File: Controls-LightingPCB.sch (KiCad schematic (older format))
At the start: 14 parts, among them J1 MinionConn, U1 LTC6820, U2 HX1188FNL

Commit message: Fixing merge issues
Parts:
- LOGO1, LOGO2: symbol utsvt-misc:Logo_Placeholder -> Controls-LightingPCB-rescue:Logo_Placeholder-utsvt-misc
- U1: symbol utsvt-chips:LTC6820 -> Controls-LightingPCB-rescue:LTC6820-utsvt-chips
- U2: symbol utsvt-chips:HX1188FNL -> Controls-LightingPCB-rescue:HX1188FNL-utsvt-chips
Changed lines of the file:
@@
 NoConn ~ 4600 4400
 $Comp
-L utsvt-chips:HX1188FNL U2
+L Controls-LightingPCB-rescue:HX1188FNL-utsvt-chips U2
 U 1 1 5F8067EF
 P 5200 4200
@@
 $EndComp
 $Comp
-L utsvt-chips:LTC6820 U1
+L Controls-LightingPCB-rescue:LTC6820-utsvt-chips U1
 U 1 1 5F8059C6
 P 5200 2650
@@
 	5950 4450 7500 4450
 $Comp
-L utsvt-misc:Logo_Placeholder LOGO2
+L Controls-LightingPCB-rescue:Logo_Placeholder-utsvt-misc LOGO2
 U 1 1 5FD2EAFC
 P 1850 3150
@@
 $EndComp
 $Comp
-L utsvt-misc:Logo_Placeholder LOGO1
+L Controls-LightingPCB-rescue:Logo_Placeholder-utsvt-misc LOGO1
 U 1 1 5FD2F351
 P 1850 2850

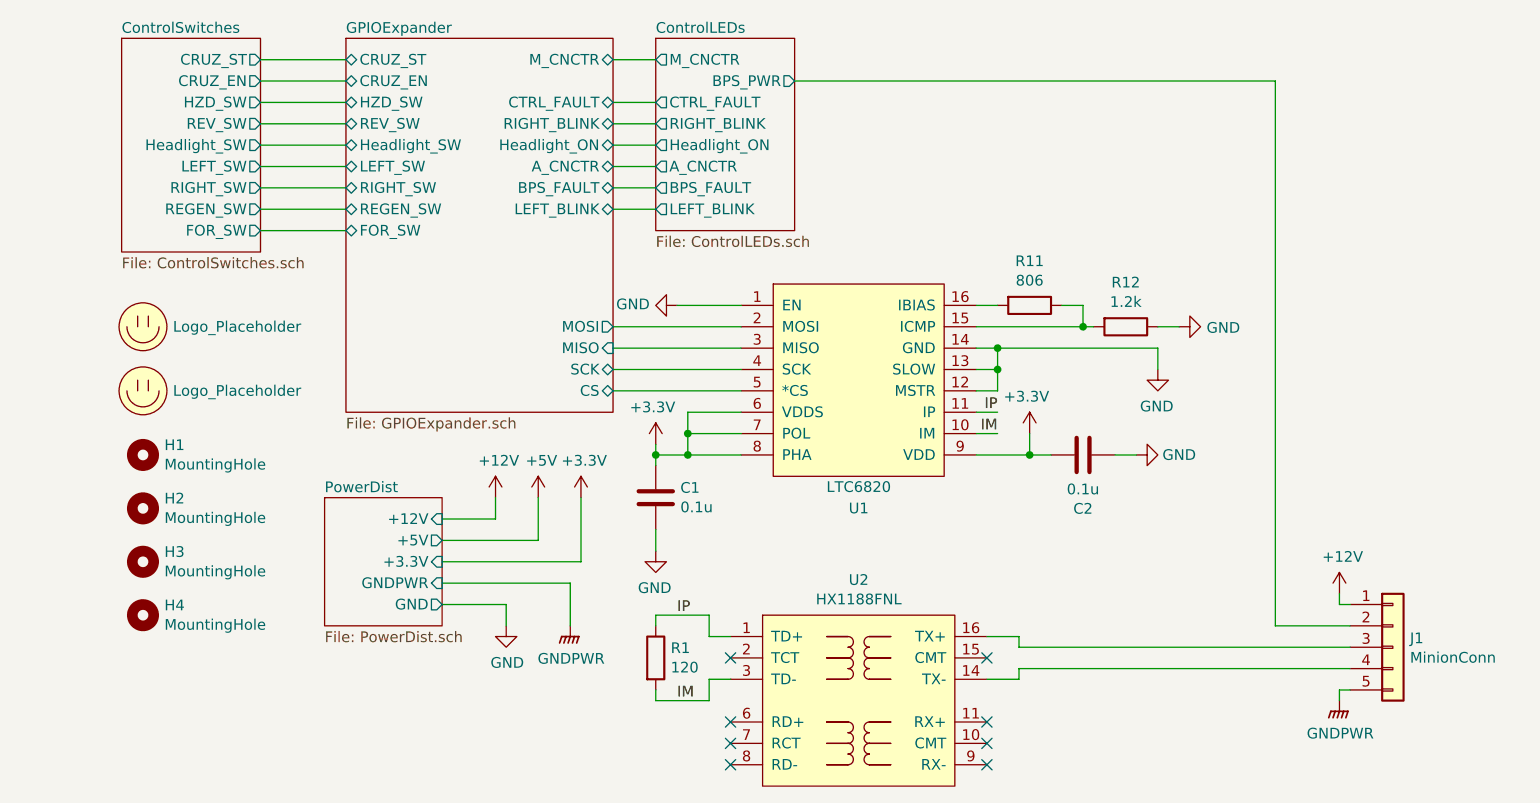
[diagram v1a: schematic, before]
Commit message: Fixed BPS_PWR lines
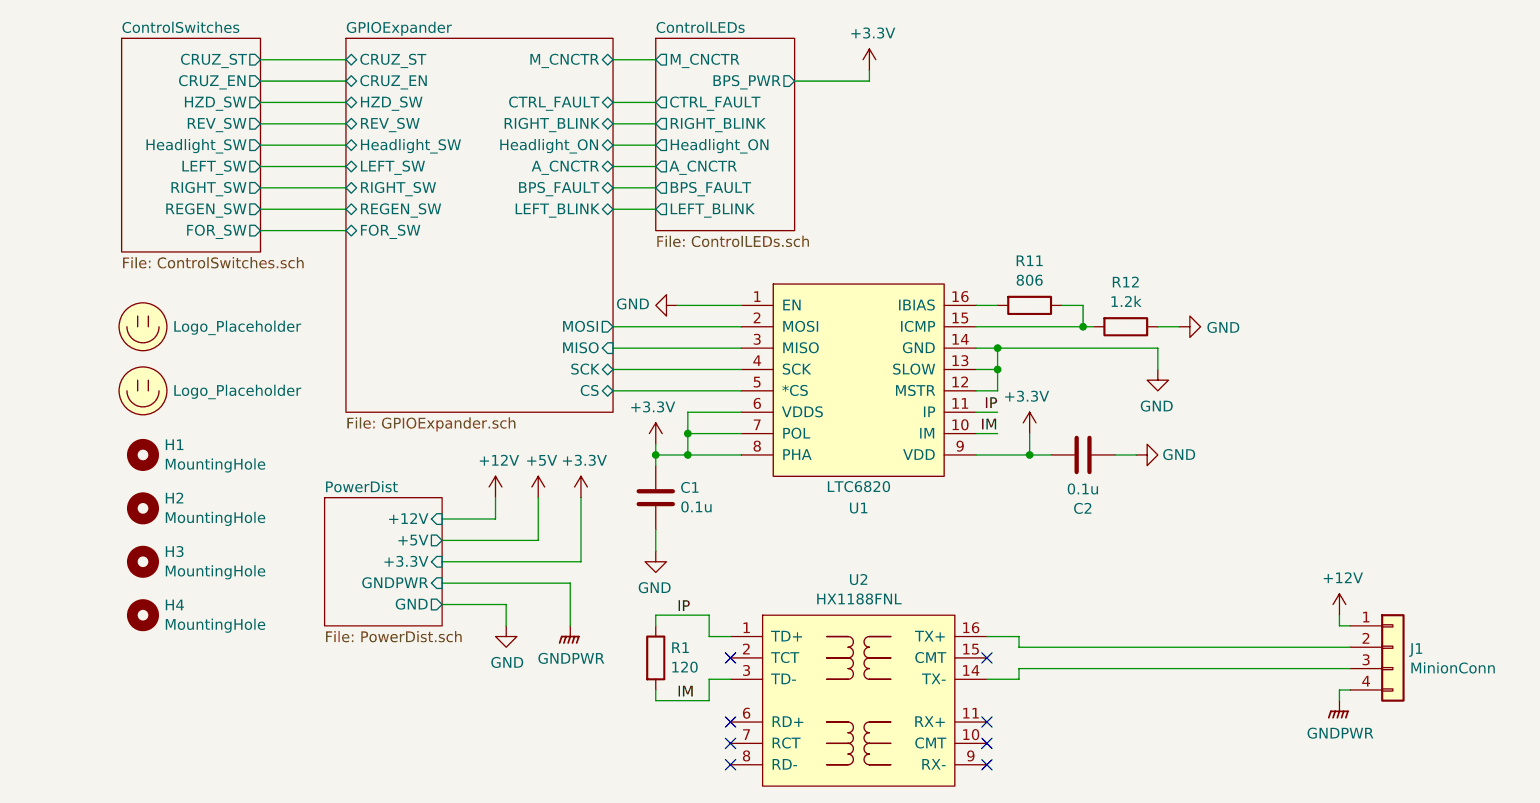
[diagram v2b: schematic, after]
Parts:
- removed J1: MinionConn, Connector_Molex:Molex_Micro-Fit_3.0_43650-0500_1x05_P3.00mm_Horizontal, symbol Connector_Generic:Conn_01x05
- added J1: MinionConn, Connector_Molex:Molex_Micro-Fit_3.0_43650-0400_1x04_P3.00mm_Horizontal, symbol Connector_Generic:Conn_01x04
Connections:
- net +12V: now also J1.1 (Pin_1)
- net GNDPWR: now also J1.4 (Pin_4)
- net at U2.14 (TX-): now also J1.3 (Pin_3)
- net at U2.16 (TX+): now also J1.2 (Pin_2)
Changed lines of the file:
@@
 L power:+12V #PWR0104
 U 1 1 5F7E142C
-P 7450 4100
-F 0 "#PWR0104" H 7450 3950 50  0001 C CNN
-F 1 "+12V" H 7465 4273 50  0000 C CNN
-F 2 "" H 7450 4100 50  0001 C CNN
-F 3 "" H 7450 4100 50  0001 C CNN
-	1    7450 4100
+P 7450 4200
+F 0 "#PWR0104" H 7450 4050 50  0001 C CNN
+F 1 "+12V" H 7465 4373 50  0000 C CNN
+F 2 "" H 7450 4200 50  0001 C CNN
+F 3 "" H 7450 4200 50  0001 C CNN
+	1    7450 4200
 	1    0    0    -1
 $EndComp
@@
 	3500 3750 3500 3650
 Wire Wire Line
-	7450 4100 7450 4150
+	7450 4200 7450 4250
 Wire Wire Line
 	7450 4550 7450 4600
@@
 Wire Wire Line
 	2400 2400 2800 2400
-$Comp
-L Connector_Generic:Conn_01x05 J1
-U 1 1 5FCAAC2B
-P 7700 4350
-F 0 "J1" H 7780 4392 50  0000 L CNN
-F 1 "MinionConn" H 7780 4301 50  0000 L CNN
-F 2 "Connector_Molex:Molex_Micro-Fit_3.0_43650-0500_1x05_P3.00mm_Horizontal" H 7700 4350 50  0001 C CNN
-F 3 "~" H 7700 4350 50  0001 C CNN
-	1    7700 4350
-	1    0    0    -1
-$EndComp
-Wire Wire Line
-	7450 4150 7500 4150
+Wire Wire Line
+	7450 4250 7500 4250
 Wire Wire Line
 	7500 4550 7450 4550
-Wire Wire Line
-	7500 4250 7150 4250
-Wire Wire Line
-	7150 4250 7150 1700
-Wire Wire Line
-	7150 1700 4900 1700
 Wire Wire Line
 	5950 4350 7500 4350
@@
 	1    0    0    -1
 $EndComp
+$Comp
+L Connector_Generic:Conn_01x04 J1
+U 1 1 5FCC2338
+P 7700 4350
+F 0 "J1" H 7780 4342 50  0000 L CNN
+F 1 "MinionConn" H 7780 4251 50  0000 L CNN
+F 2 "Connector_Molex:Molex_Micro-Fit_3.0_43650-0400_1x04_P3.00mm_Horizontal" H 7700 4350 50  0001 C CNN
+F 3 "~" H 7700 4350 50  0001 C CNN
+	1    7700 4350
+	1    0    0    -1
+$EndComp
+$Comp
+L power:+3.3V #PWR?
+U 1 1 5FCC52AA
+P 5250 1650
+F 0 "#PWR?" H 5250 1500 50  0001 C CNN
+F 1 "+3.3V" H 5265 1823 50  0000 C CNN
+F 2 "" H 5250 1650 50  0001 C CNN
+F 3 "" H 5250 1650 50  0001 C CNN
+	1    5250 1650
+	1    0    0    -1
+$EndComp
+Wire Wire Line
+	4900 1700 5250 1700
+Wire Wire Line
+	5250 1700 5250 1650
 $EndSCHEMATC
